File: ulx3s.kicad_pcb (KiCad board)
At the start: 4 copper layers, 94 x 50.8 mm, 235 parts, among them J1 CONN_02X20, J2 CONN_02X20, J3 WIFI_OFF, J4 CONN_02X03, J5 VJ1, Q1 BC857, Q2 2N7002, SW1 SW_DIP_x04, U1 LFE5U-85F-6BG381C, U10 IS25LP128F-JBLE, U11 PCA9306D, U2 MT48LC16M16A2TG, U3 TLV62569DBV, U4 TLV62569DBV, U5 TLV62569DBV, U6 FT231XQ, U7 MCP7940NT, U8 MAX11125, U9 ESP32, Y1 FNETHE025, Y2 32768Hz

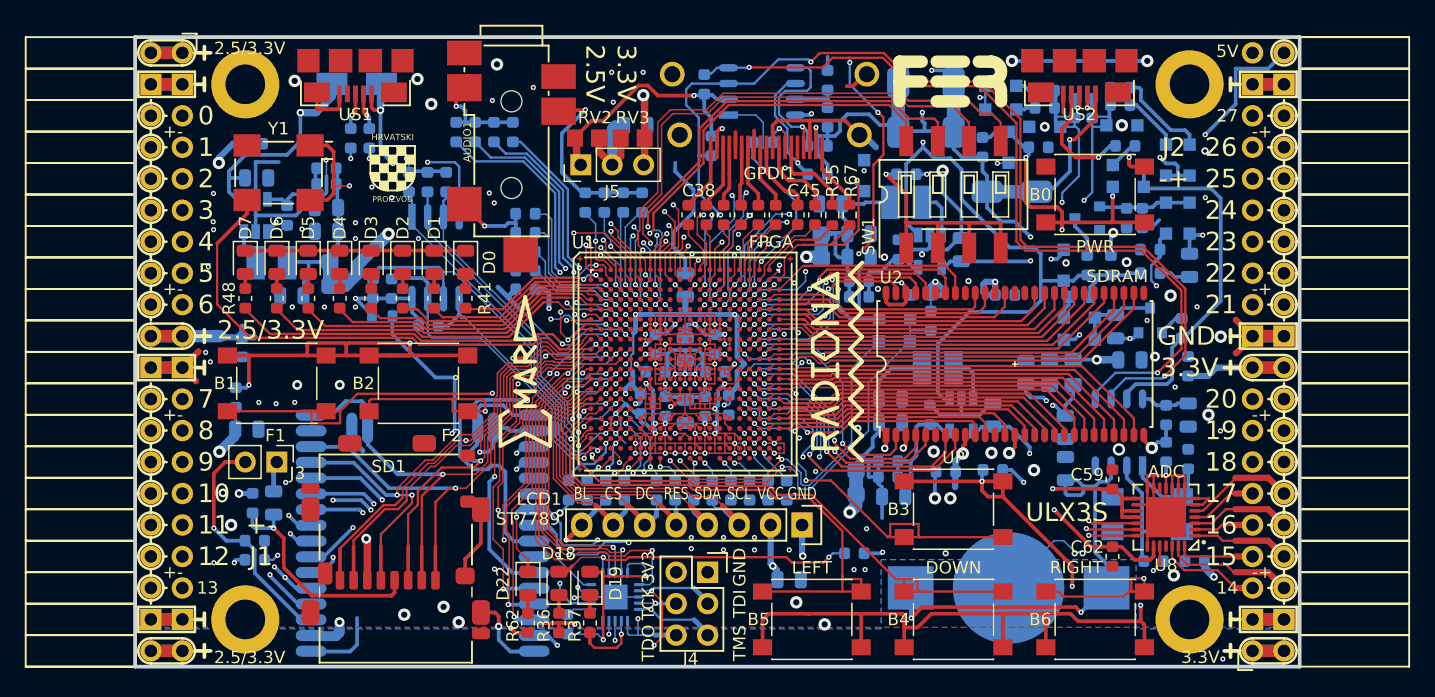
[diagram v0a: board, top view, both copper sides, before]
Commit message: Adding files for Kicad 6
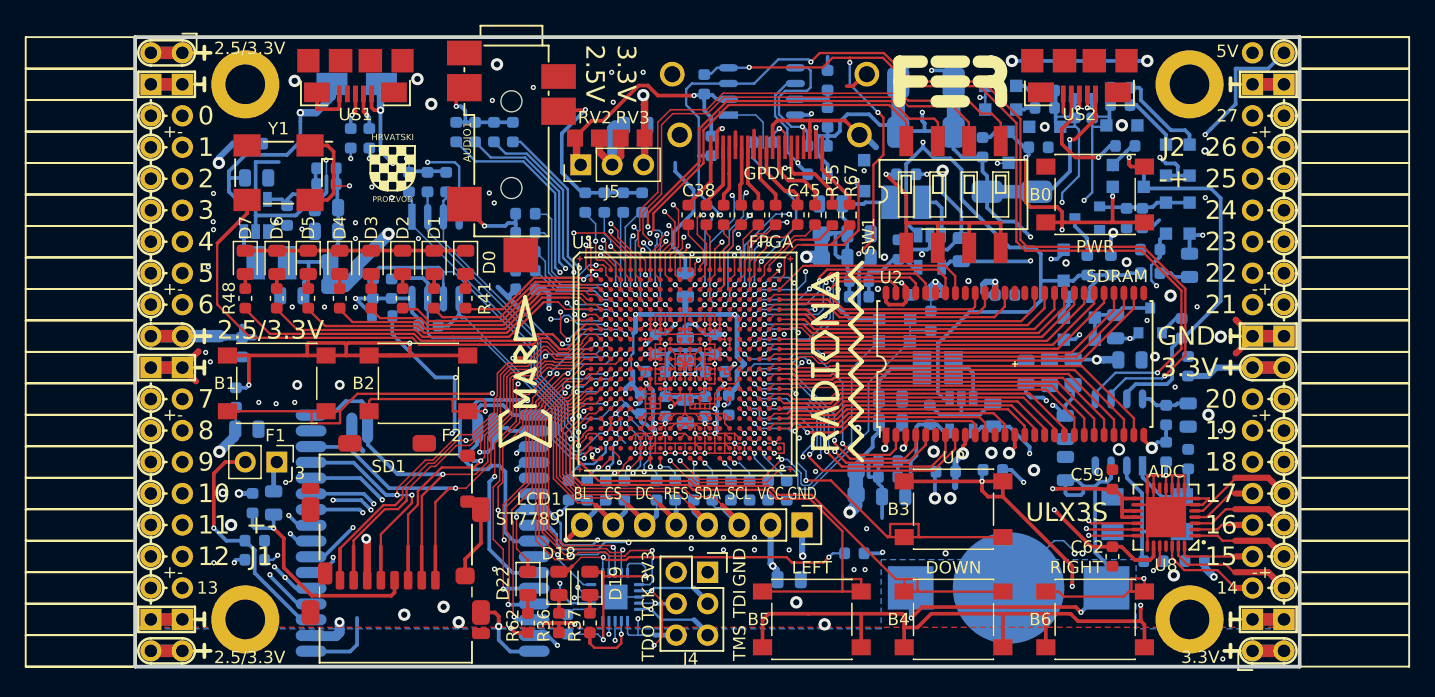
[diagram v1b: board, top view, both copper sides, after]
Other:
- net class BGA removed
- net class Default removed
- net class Medium removed
